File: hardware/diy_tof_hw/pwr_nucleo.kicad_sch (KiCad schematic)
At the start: 6 parts, among them J1 Conn_01x02_Pin, J2 Conn_01x03_Pin, U1 NUCLEO-F042K6

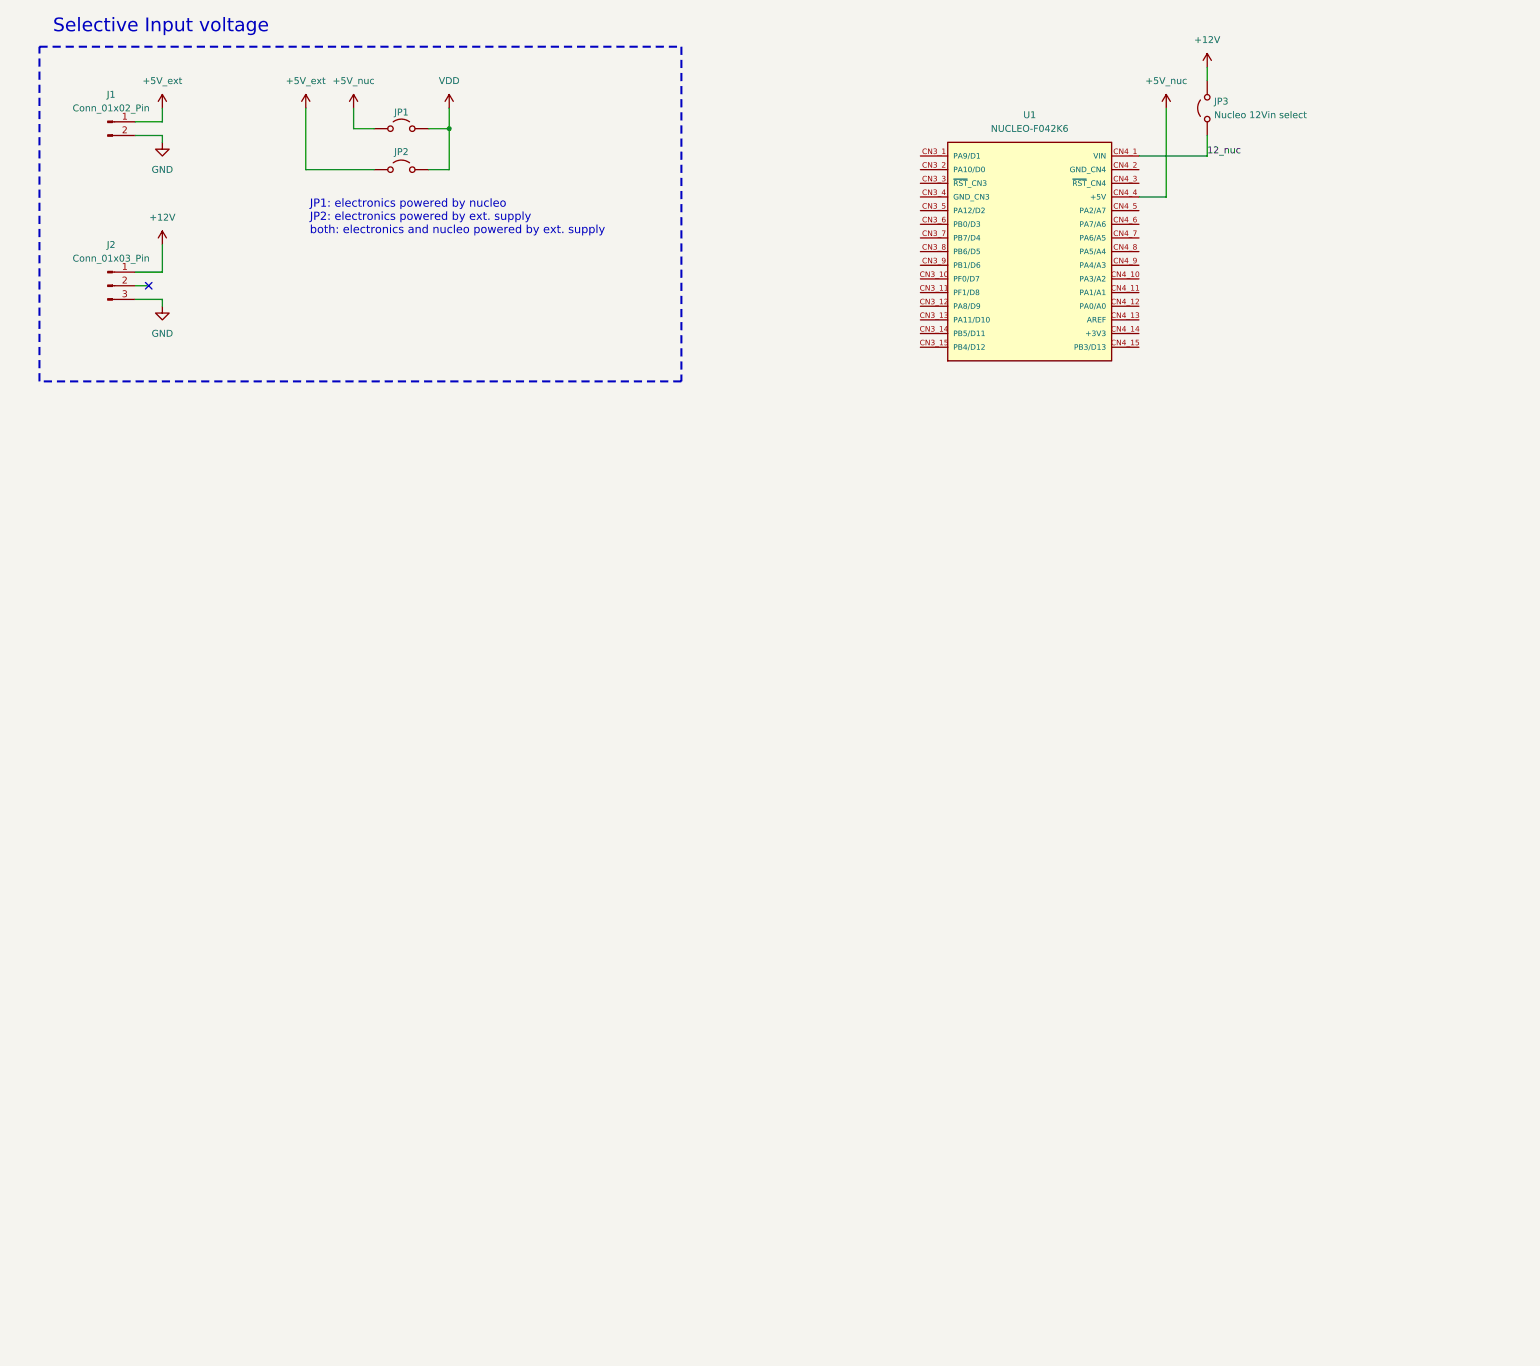
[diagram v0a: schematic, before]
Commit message: [hardware] drawn initial version of the power / nucleo sheet
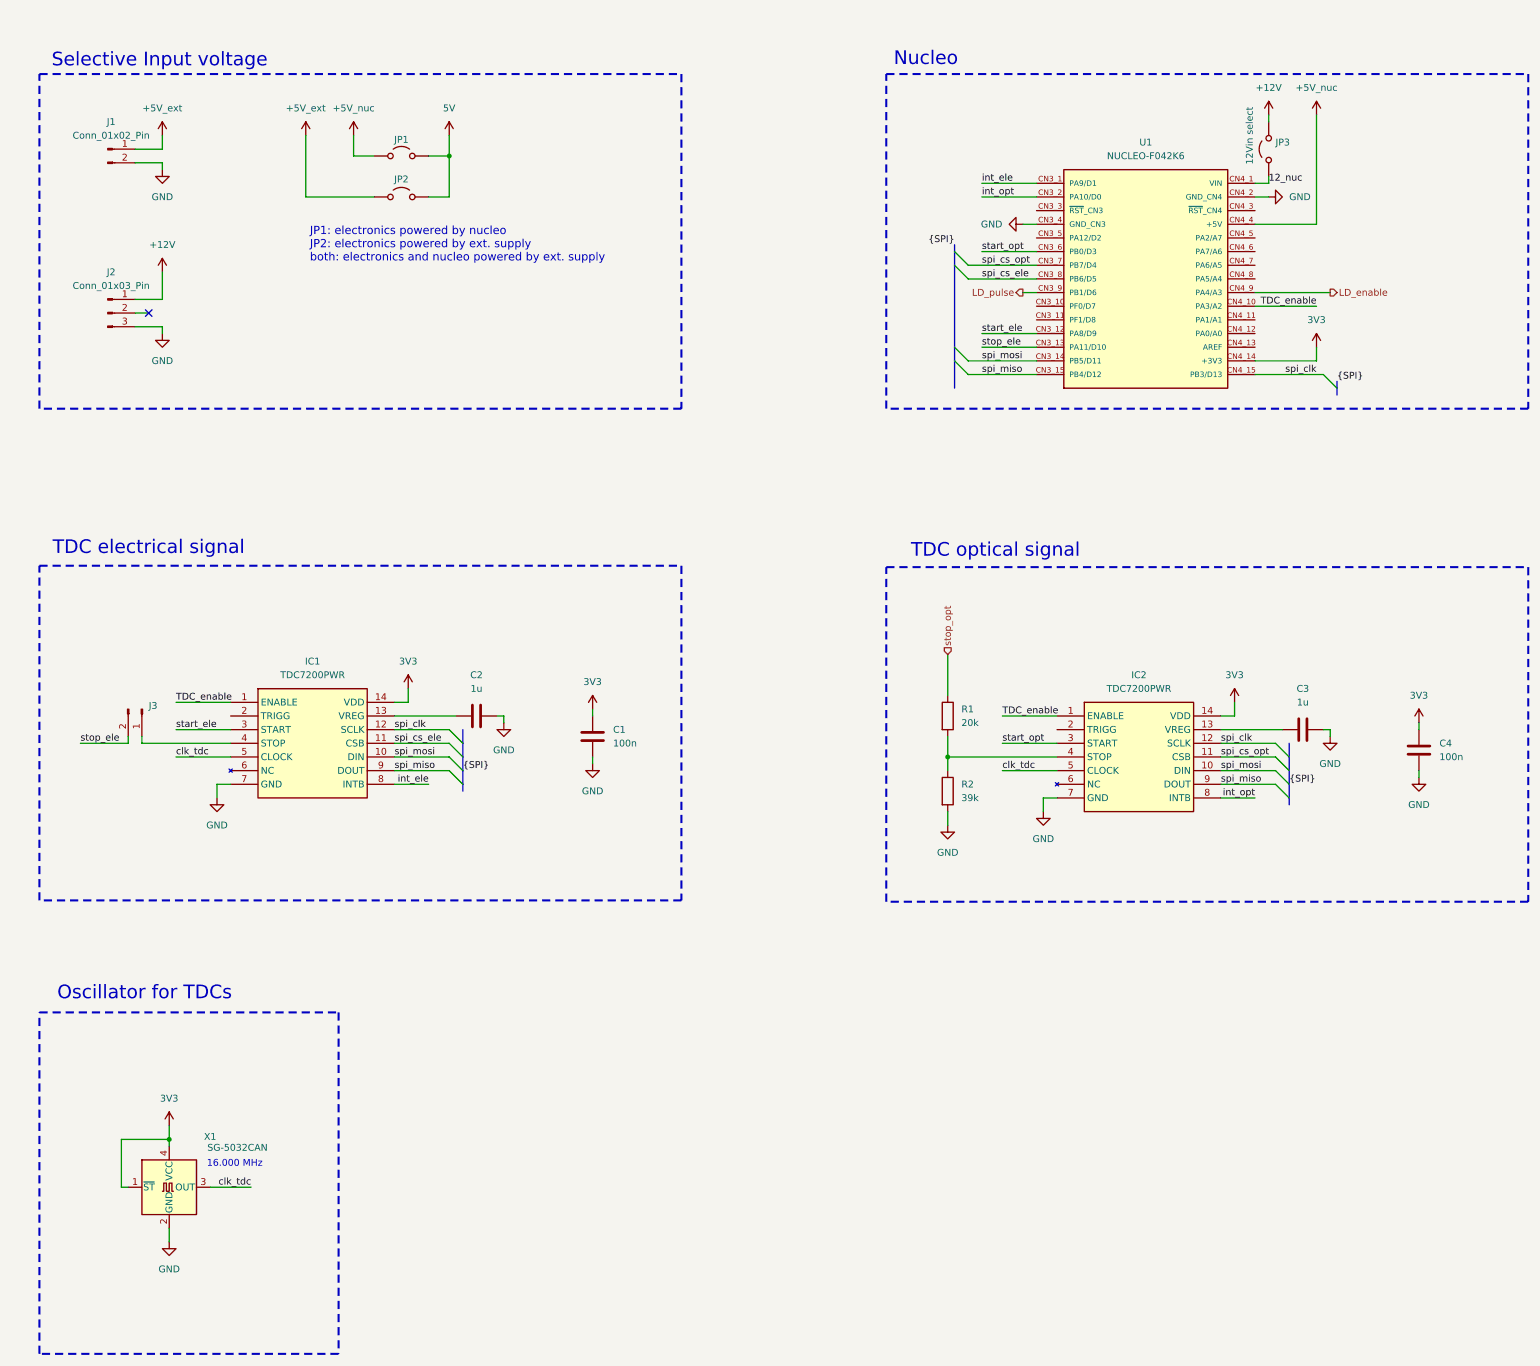
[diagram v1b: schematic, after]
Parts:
- added C1, C4: 100n, Capacitor_SMD:C_0402_1005Metric_Pad0.74x0.62mm_HandSolder, symbol Device:C
- added C2, C3: 1u, Capacitor_SMD:C_0402_1005Metric_Pad0.74x0.62mm_HandSolder, symbol Device:C
- added IC1, IC2: TDC7200PWR, SOP65P640X120-14N, symbol TDC7200PWR:TDC7200PWR
- added J3: Conn_01x02_Pin, Connector_Molex:Molex_KK-254_AE-6410-02A_1x02_P2.54mm_Vertical, symbol Connector:Conn_01x02_Pin
- added R1: 20k, Resistor_SMD:R_0603_1608Metric_Pad0.98x0.95mm_HandSolder, symbol Device:R
- added R2: 39k, Resistor_SMD:R_0603_1608Metric_Pad0.98x0.95mm_HandSolder, symbol Device:R
- added X1: SG-5032CAN, Oscillator:Oscillator_SMD_SeikoEpson_SG8002LB-4Pin_5.0x3.2mm_HandSoldering, symbol Oscillator:SG-5032CAN
- JP3: value Nucleo 12Vin select -> 12Vin select
- U1: footprint NUCLEO-F042K6:MODULE_NUCLEO-F042K6 -> NUCLEO_F042K6:MODULE_NUCLEO-F042K6
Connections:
- net GND: now also U1.CN3_4 (GND_CN3), U1.CN4_2 (GND_CN4), C1.2, C2.2, C3.2, C4.2, IC1.7 (GND), IC2.7 (GND), R2.2, X1.2 (GND)
- net int_ele: now reaches U1.CN3_1 (PA9/D1)
- net int_ele: now also IC1.8 (INTB)
- net start_ele: now reaches U1.CN3_12 (PA8/D9)
- net start_ele: now also IC1.3 (START)
- net stop_ele: now reaches U1.CN3_13 (PA11/D10)
- net stop_ele: now also J3.2 (Pin_2)
- net spi_mosi: now reaches U1.CN3_14 (PB5/D11)
- net spi_mosi: now also IC1.10 (DIN), IC2.10 (DIN)
- net spi_miso: now reaches U1.CN3_15 (PB4/D12)
- net spi_miso: now also IC1.9 (DOUT), IC2.9 (DOUT)
- net int_opt: now reaches U1.CN3_2 (PA10/D0)
- net int_opt: now also IC2.8 (INTB)
- net start_opt: now reaches U1.CN3_6 (PB0/D3)
- net start_opt: now also IC2.3 (START)
- net spi_cs_opt: now reaches U1.CN3_7 (PB7/D4)
- net spi_cs_opt: now also IC2.11 (CSB)
- net spi_cs_ele: now reaches U1.CN3_8 (PB6/D5)
- net spi_cs_ele: now also IC1.11 (CSB)
- net LD_pulse: now reaches U1.CN3_9 (PB1/D6)
- net TDC_enable: now reaches U1.CN4_10 (PA3/A2)
- net TDC_enable: now also IC1.1 (ENABLE), IC2.1 (ENABLE)
- net 3V3: now reaches U1.CN4_14 (+3V3)
- net 3V3: now also C1.1, C4.1, IC1.14 (VDD), IC2.14 (VDD), X1.1 (~{ST}), X1.4 (VCC)
- net spi_clk: now reaches U1.CN4_15 (PB3/D13)
- net spi_clk: now also IC1.12 (SCLK), IC2.12 (SCLK)
- net LD_enable: now reaches U1.CN4_9 (PA4/A3)
- net VDD renamed 5V
- new net: C2.1, IC1.13 (VREG)
- new net: IC1.4 (STOP), J3.1 (Pin_1)
- new net: C3.1, IC2.13 (VREG)
- new net: IC2.4 (STOP), R1.2, R2.1
- new net clk_tdc: IC1.5 (CLOCK), IC2.5 (CLOCK), X1.3 (OUT)
- new net stop_opt: R1.1
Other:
- note added: "16.000 MHz"
- note added: "Nucleo"
- note added: "Oscillator for TDCs"
- note added: "TDC electrical signal"
- note added: "TDC optical signal"
- title: (none) -> Power, Nucleo, TDC
- moved on the sheet: J1, J2, JP1, JP2, JP3, U1

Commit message: [hardware] added schematics and library components for the laser driver as well as TIA circuit
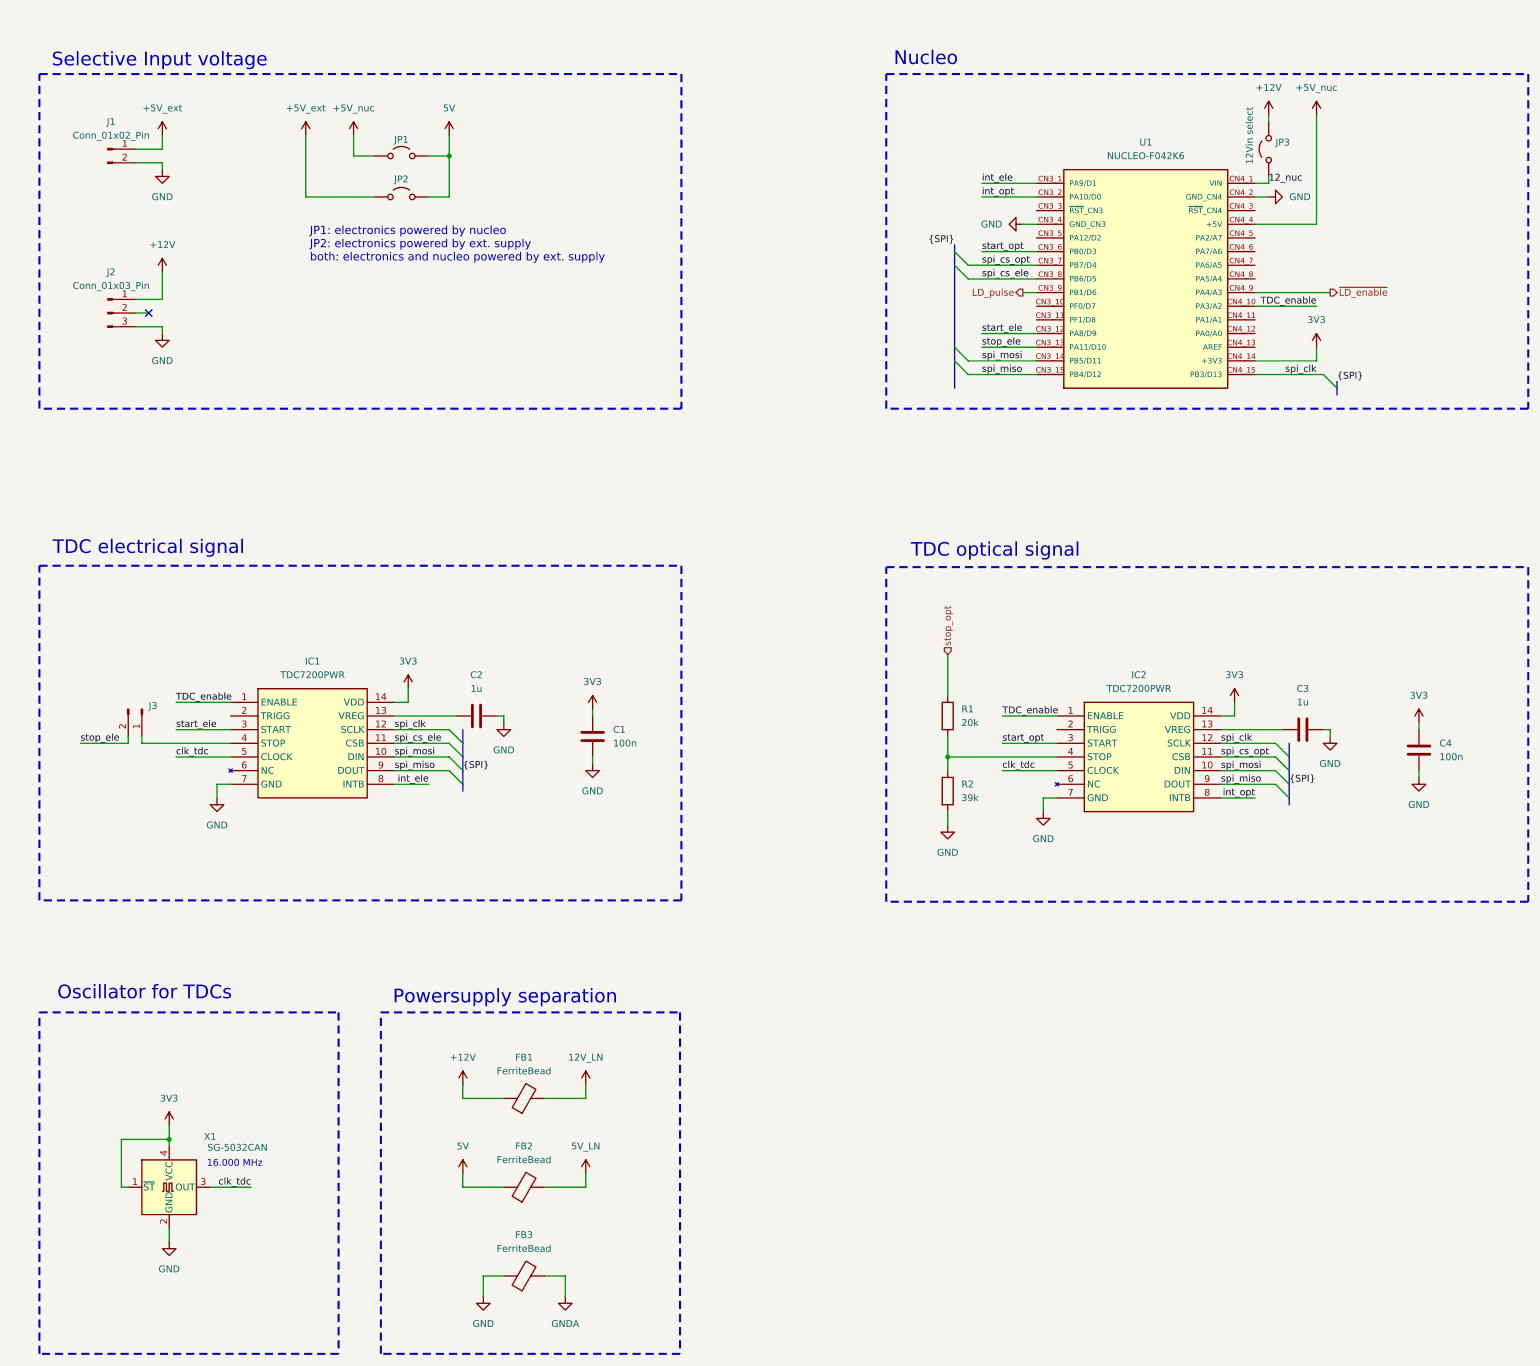
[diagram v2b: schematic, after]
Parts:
- added FB1, FB2, FB3: FerriteBead, Inductor_SMD:L_0402_1005Metric_Pad0.77x0.64mm_HandSolder, symbol Device:FerriteBead
- R1, R2: footprint Resistor_SMD:R_0603_1608Metric_Pad0.98x0.95mm_HandSolder -> Resistor_SMD:R_0402_1005Metric_Pad0.72x0.64mm_HandSolder
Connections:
- net +12V: now also FB1.1
- net 5V: now also FB2.1
- net GND: now also FB3.1
- net LD_enable renamed ~{LD_enable}
- new net 12V_LN: FB1.2
- new net 5V_LN: FB2.2
- new net GNDA: FB3.2
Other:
- note added: "Powersupply separation"

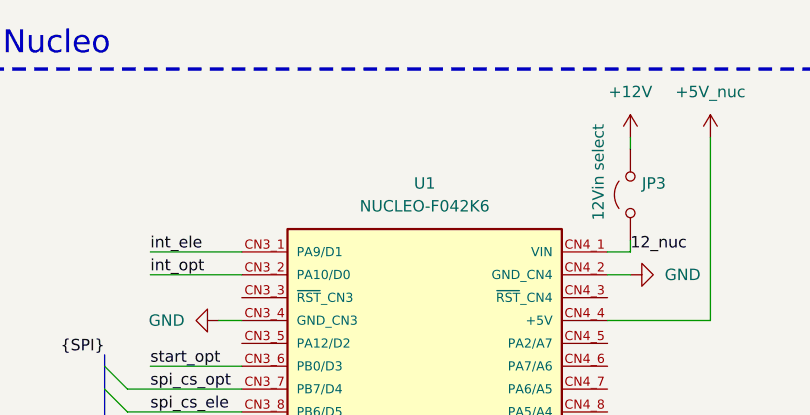
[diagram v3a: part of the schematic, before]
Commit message: [hardware] cherry picked changes from review
[hardware] add description text for JP3

Signed-off-by: Timon Burkard <burkard.timon@gmail.com>
(cherry picked from commit 44d5712227eb7a57076d25d490ffb1ca2a138412)

[hardware] use relative path for schematics template

Signed-off-by: Timon Burkard <burkard.timon@gmail.com>
(cherry picked from commit 5e7c5f0f6d85de52cfba936180bf5f2080214473)

[hardware] use explicit path to STEP files for U1, IC1, IC2, IC21, IC22

Signed-off-by: Timon Burkard <burkard.timon@gmail.com>
(cherry picked from commit 2ea5c7e3506b8eddbb4935cb7e42b338c20b0635)
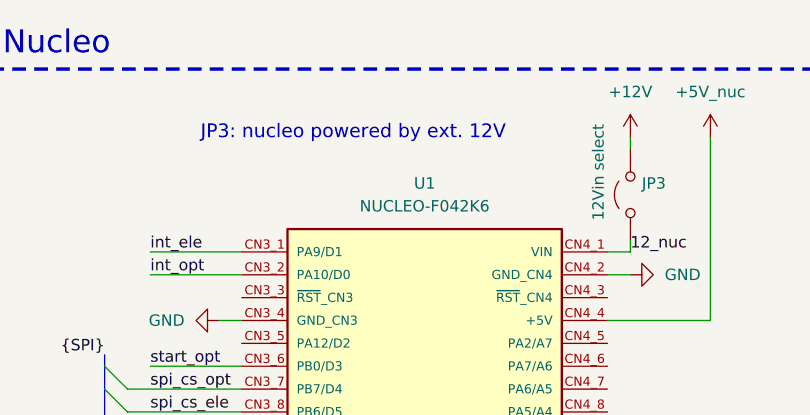
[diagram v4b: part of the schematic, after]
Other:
- note added: "JP3: nucleo powered by ext. 12V"
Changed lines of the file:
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@@
+		)
+	)
+	(text "JP3: nucleo powered by ext. 12V"
+		(exclude_from_sim no)
+		(at 213.868 32.512 0)
+		(effects
+			(font
+				(size 1.524 1.524)
+			)
+			(justify left)
 		)
 	)
